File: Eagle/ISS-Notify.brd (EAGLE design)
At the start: 63.5 x 63.5 mm, 54 parts, among them J1 AVRISP, J2 JST2, J3 PROTOSPACE2, SW1 9077-1, SW2 SWITCH, U1 ATMEGA32U4, U2 MCP7940N, U3 TPS63001, U4 MCP73811, U5 TLC5971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

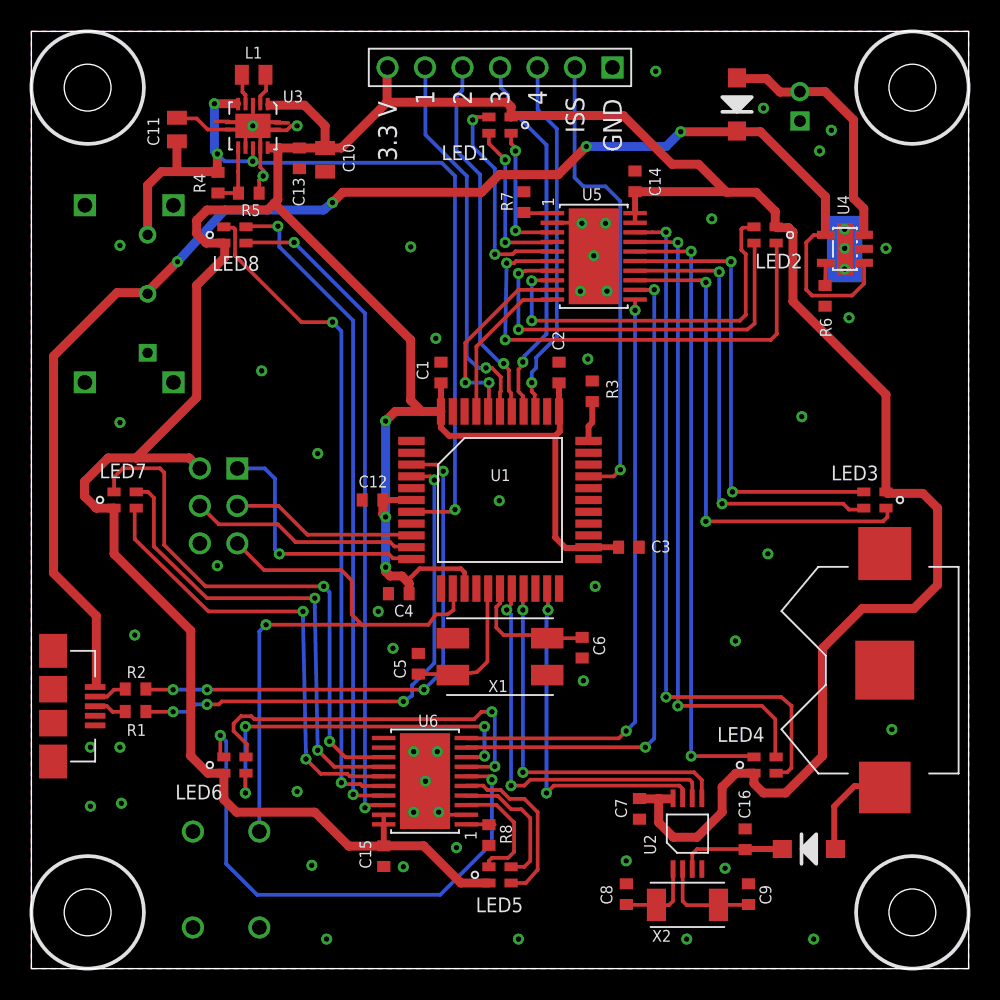
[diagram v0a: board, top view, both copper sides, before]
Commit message: edge ground place stipling
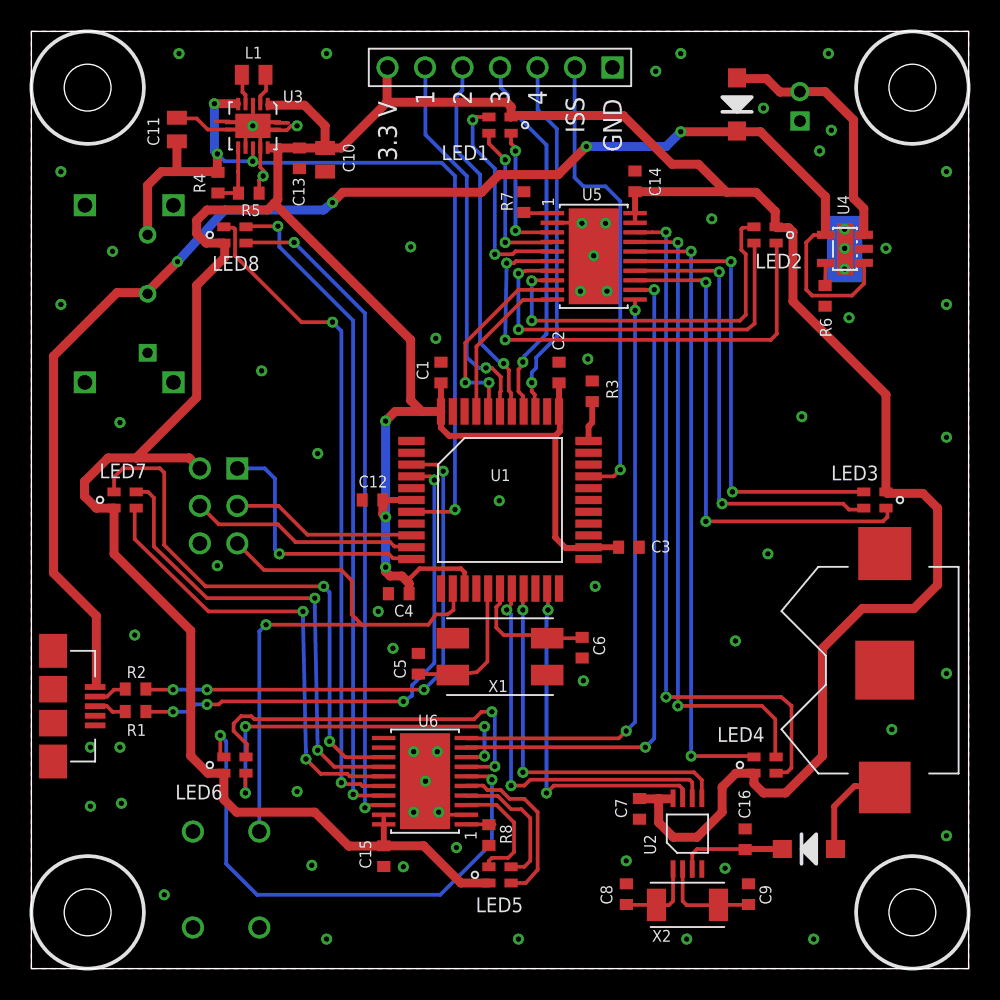
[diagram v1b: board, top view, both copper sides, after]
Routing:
- net GND: vias 52 -> 64
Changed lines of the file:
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@@
 <setting verticaltext="up"/>
 </settings>
-<grid distance="0.1" unitdist="mm" unit="mm" style="lines" multiple="1" display="yes" altdistance="0.025" altunitdist="inch" altunit="inch"/>
+<grid distance="1" unitdist="mm" unit="mm" style="lines" multiple="1" display="yes" altdistance="0.025" altunitdist="inch" altunit="inch"/>
 <layers>
 <layer number="1" name="Top" color="4" fill="1" visible="yes" active="yes"/>
@@
 <via x="15.6" y="40.5" extent="1-16" drill="0.36"/>
 <via x="6" y="37" extent="1-16" drill="0.36"/>
-<via x="6" y="49" extent="1-16" drill="0.36"/>
+<via x="5.5" y="48.6" extent="1-16" drill="0.36"/>
 <via x="4" y="15" extent="1-16" drill="0.36"/>
 <via x="6" y="15" extent="1-16" drill="0.36"/>
@@
 <wire x1="37.265" y1="50.535" x2="37.3" y2="50.5" width="0.254" layer="1"/>
 <via x="12.6" y="27.3" extent="1-16" drill="0.36"/>
+<via x="2" y="45" extent="1-16" drill="0.36"/>
+<via x="2" y="54" extent="1-16" drill="0.36"/>
+<via x="10" y="62" extent="1-16" drill="0.36"/>
+<via x="20" y="62" extent="1-16" drill="0.36"/>
+<via x="44" y="62" extent="1-16" drill="0.36"/>
+<via x="54" y="62" extent="1-16" drill="0.36"/>
+<via x="62" y="54" extent="1-16" drill="0.36"/>
+<via x="62" y="45" extent="1-16" drill="0.36"/>
+<via x="62" y="36" extent="1-16" drill="0.36"/>
+<via x="62" y="20" extent="1-16" drill="0.36"/>
+<via x="62" y="9" extent="1-16" drill="0.36"/>
+<via x="9" y="5" extent="1-16" drill="0.36"/>
 </signal>
 <signal name="VCC">

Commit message: drc passed
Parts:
- moved C16 0.30 mm to (48.4, 8.47)
- moved U2 0.30 mm to (44.5, 8.84)
- moved C8 0.30 mm to (40.3, 4.74)
- moved C9 0.30 mm to (48.6, 4.74)
- moved X2 0.30 mm to (44.5, 4.02)
- moved C7 0.30 mm to (41.2, 10.5)
- moved D2 0.30 mm to (52.7, 7.80)
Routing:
- net GND: track 23.1 -> 21.3 mm
- net N$41: track 44.9 -> 46.1 mm
- net N$35: track 26.4 -> 27.4 mm
- net VCC: track 282.7 -> 283.4 mm

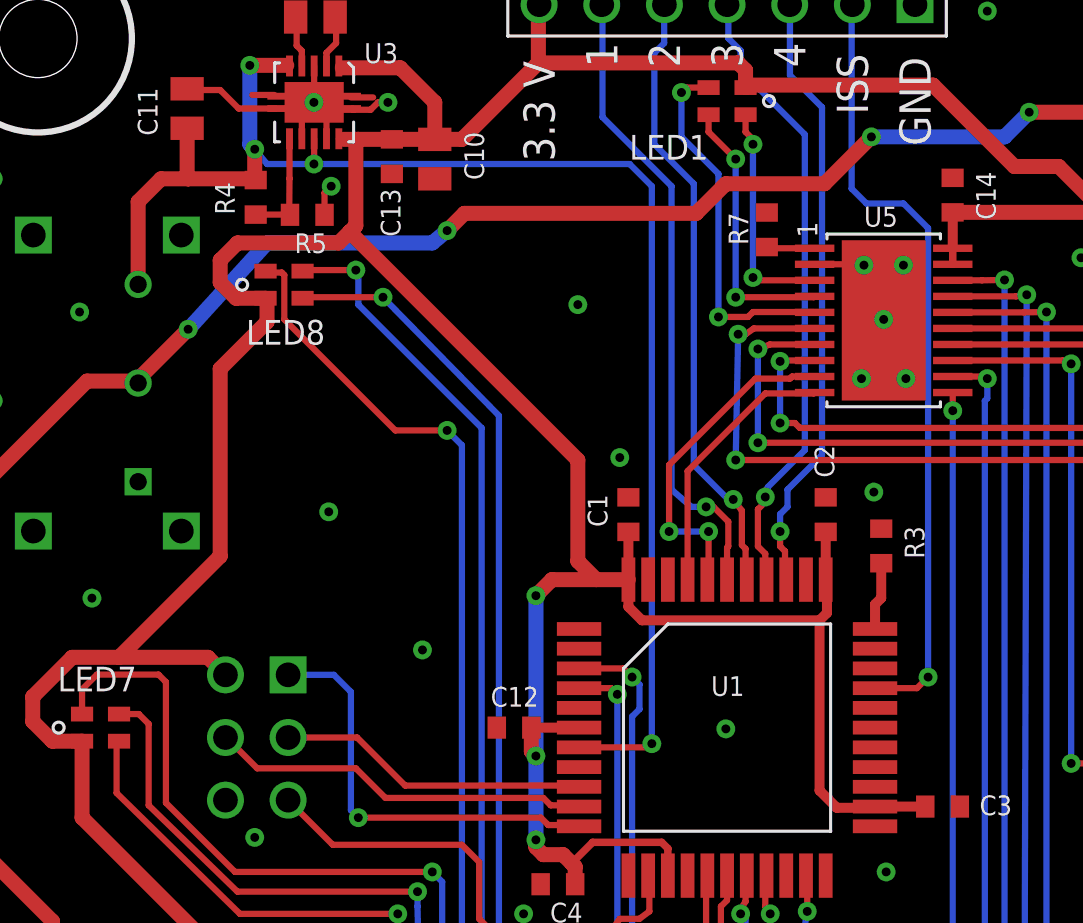
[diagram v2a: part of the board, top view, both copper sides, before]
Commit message: bat sense signal
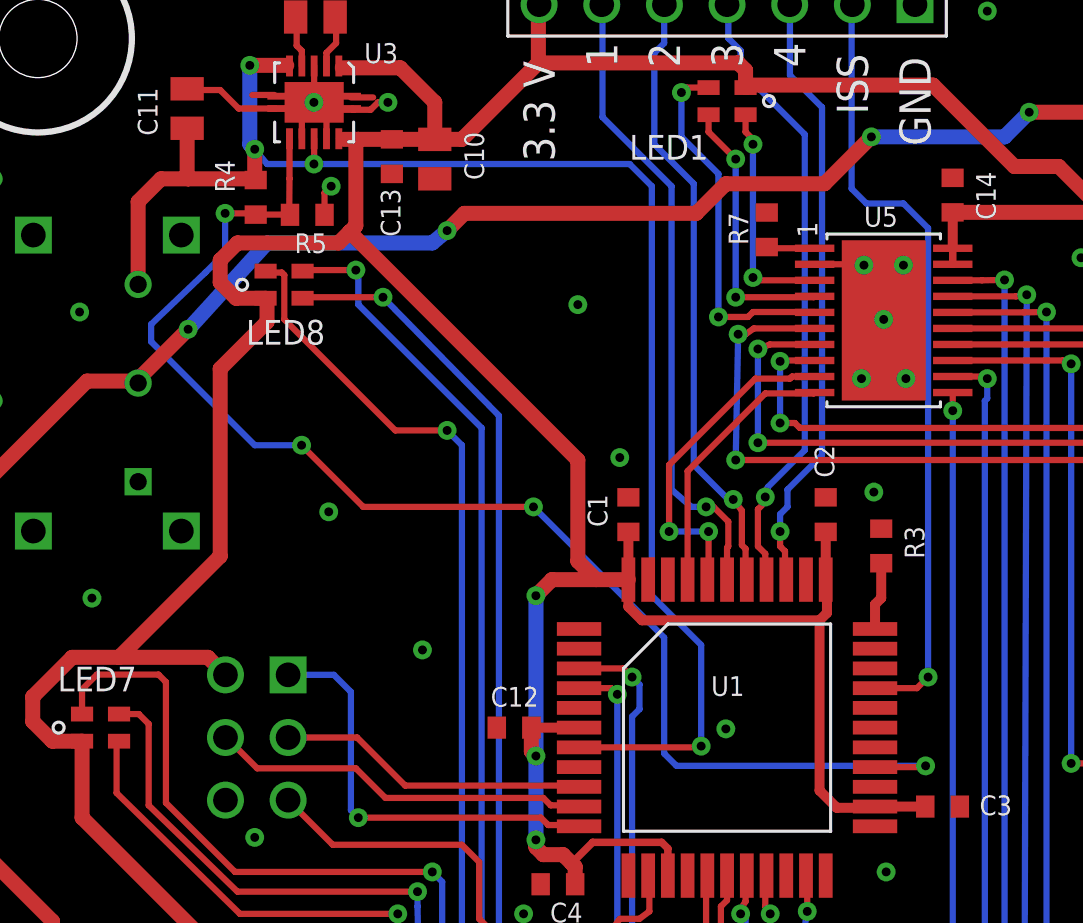
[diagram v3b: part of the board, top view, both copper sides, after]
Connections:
- removed net N$3: R4.1, R5.2, U3.6
- new net BATSENSE: R4.1, R5.2, U1.26, U3.6
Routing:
- net BATSENSE: track 0.00 -> 55.7 mm, vias 0 -> 4
- net N$3: track 4.63 -> 0.00 mm
- net VIN: track 60.3 -> 63.2 mm
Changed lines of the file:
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@@
 </element>
 <element name="R4" library="rcl_custom" package="0603-C-NOSILK" value="39 k" x="12.64" y="53.25" smashed="yes" rot="R90">
-<attribute name="NAME" x="11.79" y="52.55" size="0.8" layer="25" font="vector" ratio="20" rot="R90"/>
+<attribute name="NAME" x="11.79" y="53.45" size="0.8" layer="25" font="vector" ratio="20" rot="R90"/>
 <attribute name="VALUE" x="14.64" y="52.45" size="1" layer="27" ratio="10" rot="R90"/>
 </element>
@@
 <wire x1="15.9" y1="59.5" x2="15.9" y2="60.62" width="0.254" layer="1"/>
 <wire x1="15.9" y1="60.62" x2="15.86" y2="60.56" width="0.254" layer="1"/>
-</signal>
-<signal name="N$3">
-<contactref element="R4" pad="1"/>
-<contactref element="R5" pad="2"/>
-<contactref element="U3" pad="6"/>
-<wire x1="12.64" y1="52.55" x2="13.92" y2="52.55" width="0.254" layer="1"/>
-<wire x1="13.92" y1="52.55" x2="14.03" y2="52.54" width="0.254" layer="1"/>
-<wire x1="14.01" y1="55.625" x2="14.01" y2="54.01" width="0.254" layer="1"/>
-<wire x1="14.01" y1="54.01" x2="14" y2="52.7" width="0.254" layer="1"/>
-<wire x1="14" y1="52.7" x2="13.9" y2="52.71" width="0.254" layer="1"/>
-<wire x1="13.9" y1="52.71" x2="14.03" y2="52.54" width="0.254" layer="1"/>
 </signal>
 <signal name="VIN">
@@
 <wire x1="15" y1="54.6" x2="13.1" y2="54.6" width="0.254" layer="16"/>
 <wire x1="13.1" y1="54.6" x2="12.6" y2="55.2" width="0.254" layer="16"/>
-<wire x1="25.75" y1="30.95" x2="28.55" y2="30.95" width="0.254" layer="1"/>
-<wire x1="28.55" y1="30.95" x2="28.7" y2="31.1" width="0.254" layer="1"/>
-<via x="28.7" y="31.1" extent="1-16" drill="0.36"/>
+<wire x1="25.75" y1="30.95" x2="30.55" y2="30.95" width="0.254" layer="1"/>
+<wire x1="30.55" y1="30.95" x2="30.7" y2="31" width="0.254" layer="1"/>
+<via x="30.7" y="31" extent="1-16" drill="0.36"/>
 <wire x1="15" y1="54.6" x2="27.8" y2="54.6" width="0.254" layer="16"/>
 <wire x1="27.8" y1="54.6" x2="28.7" y2="53.7" width="0.254" layer="16"/>
-<wire x1="28.7" y1="53.7" x2="28.7" y2="31.1" width="0.254" layer="16"/>
+<wire x1="30.7" y1="31" x2="30.7" y2="35.1" width="0.254" layer="16"/>
+<wire x1="30.7" y1="35.1" x2="28.7" y2="37.1" width="0.254" layer="16"/>
+<wire x1="28.7" y1="37.1" x2="28.7" y2="53.7" width="0.254" layer="16"/>
 </signal>
 <signal name="GND">
@@
 <via x="55.1" y="47.4" extent="1-16" drill="0.36"/>
 </signal>
+<signal name="BATSENSE">
+<contactref element="U1" pad="26"/>
+<contactref element="R4" pad="1"/>
+<contactref element="R5" pad="2"/>
+<contactref element="U3" pad="6"/>
+<wire x1="12.64" y1="52.55" x2="13.92" y2="52.55" width="0.254" layer="1"/>
+<wire x1="13.92" y1="52.55" x2="14.03" y2="52.54" width="0.254" layer="1"/>
+<wire x1="14.01" y1="55.625" x2="14.01" y2="54.01" width="0.254" layer="1"/>
+<wire x1="14.01" y1="54.01" x2="14" y2="52.7" width="0.254" layer="1"/>
+<wire x1="14" y1="52.7" x2="13.9" y2="52.71" width="0.254" layer="1"/>
+<wire x1="13.9" y1="52.71" x2="14.03" y2="52.54" width="0.254" layer="1"/>
+<wire x1="37.75" y1="30.15" x2="39.75" y2="30.15" width="0.254" layer="1"/>
+<wire x1="39.75" y1="30.15" x2="39.8" y2="30.2" width="0.254" layer="1"/>
+<via x="39.8" y="30.2" extent="1-16" drill="0.36"/>
+<wire x1="39.8" y1="30.2" x2="29.7" y2="30.2" width="0.254" layer="16"/>
+<wire x1="29.7" y1="30.2" x2="29.2" y2="30.7" width="0.254" layer="16"/>
+<wire x1="29.2" y1="30.7" x2="29.2" y2="35.4" width="0.254" layer="16"/>
+<wire x1="29.2" y1="35.4" x2="23.9" y2="40.7" width="0.254" layer="16"/>
+<via x="23.9" y="40.7" extent="1-16" drill="0.36"/>
+<wire x1="23.9" y1="40.7" x2="17" y2="40.7" width="0.254" layer="1"/>
+<wire x1="17" y1="40.7" x2="14.5" y2="43.2" width="0.254" layer="1"/>
+<via x="14.5" y="43.2" extent="1-16" drill="0.36"/>
+<wire x1="14.5" y1="43.2" x2="12.6" y2="43.2" width="0.254" layer="16"/>
+<wire x1="12.6" y1="43.2" x2="8.4" y2="47.4" width="0.254" layer="16"/>
+<wire x1="8.4" y1="47.4" x2="8.4" y2="48.1" width="0.254" layer="16"/>
+<wire x1="8.4" y1="48.1" x2="10.6" y2="50.2" width="0.254" layer="16"/>
+<wire x1="10.6" y1="50.2" x2="11.4" y2="51" width="0.254" layer="16"/>
+<wire x1="11.4" y1="51" x2="11.4" y2="52.6" width="0.254" layer="16"/>
+<via x="11.4" y="52.6" extent="1-16" drill="0.36"/>
+<wire x1="11.4" y1="52.6" x2="12.59" y2="52.6" width="0.254" layer="1"/>
+<wire x1="12.59" y1="52.6" x2="12.64" y2="52.55" width="0.254" layer="1"/>
+</signal>
 </signals>

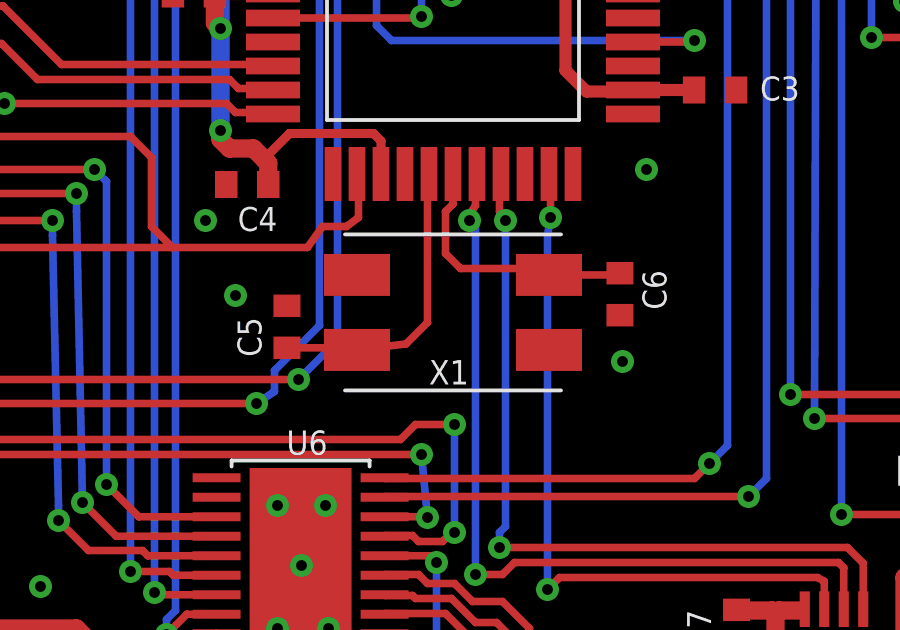
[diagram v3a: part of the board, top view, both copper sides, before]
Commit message: connect X1 pads
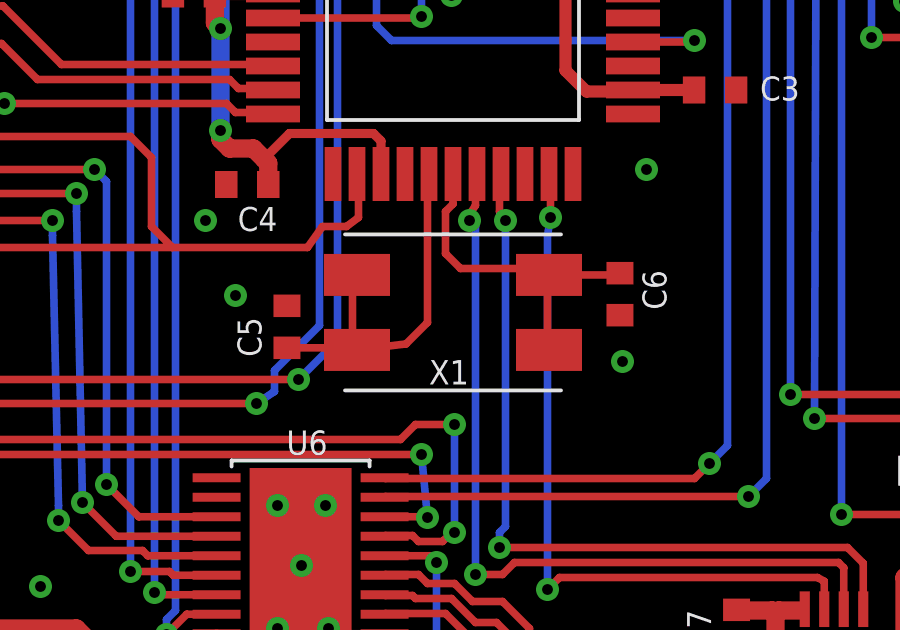
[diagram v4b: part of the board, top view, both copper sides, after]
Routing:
- net N$45: track 0.00 -> 2.90 mm
- net N$3: track 0.00 -> 2.60 mm
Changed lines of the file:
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@@
 <wire x1="12.59" y1="52.6" x2="12.64" y2="52.55" width="0.254" layer="1"/>
+</signal>
+<signal name="N$3">
+<wire x1="34.9" y1="19.8" x2="34.9" y2="22.4" width="0.254" layer="1"/>
+</signal>
+<signal name="N$45">
+<wire x1="28.4" y1="19.6" x2="28.4" y2="22.5" width="0.254" layer="1"/>
 </signal>
 </signals>

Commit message: logo
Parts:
- added U$5: V0.3, ISS-Notify:LOGO
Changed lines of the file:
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@@
 <attribute name="VALUE" x="50.36" y="7.666" size="1" layer="27" ratio="10" rot="R90"/>
 </element>
+<element name="U$5" library="ISS-Notify" package="LOGO" value="V0.3" x="40.7" y="35.5"/>
 </elements>
 <signals>
@@
 <via x="31.7" y="31.7" extent="1-16" drill="0.36"/>
 <via x="38.2" y="25.9" extent="1-16" drill="0.36"/>
-<via x="52.2" y="37.4" extent="1-16" drill="0.36"/>
+<via x="52.8" y="40.2" extent="1-16" drill="0.36"/>
 <via x="55.4" y="44.1" extent="1-16" drill="0.36"/>
 <via x="46.1" y="50.8" extent="1-16" drill="0.36"/>
